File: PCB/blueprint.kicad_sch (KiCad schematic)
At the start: 7 parts, among them SW1 SW_Push, SW2 SW_Push, SW3 SW_Push, SW4 SW_Push, U1 XIAO-RP2040-DIP

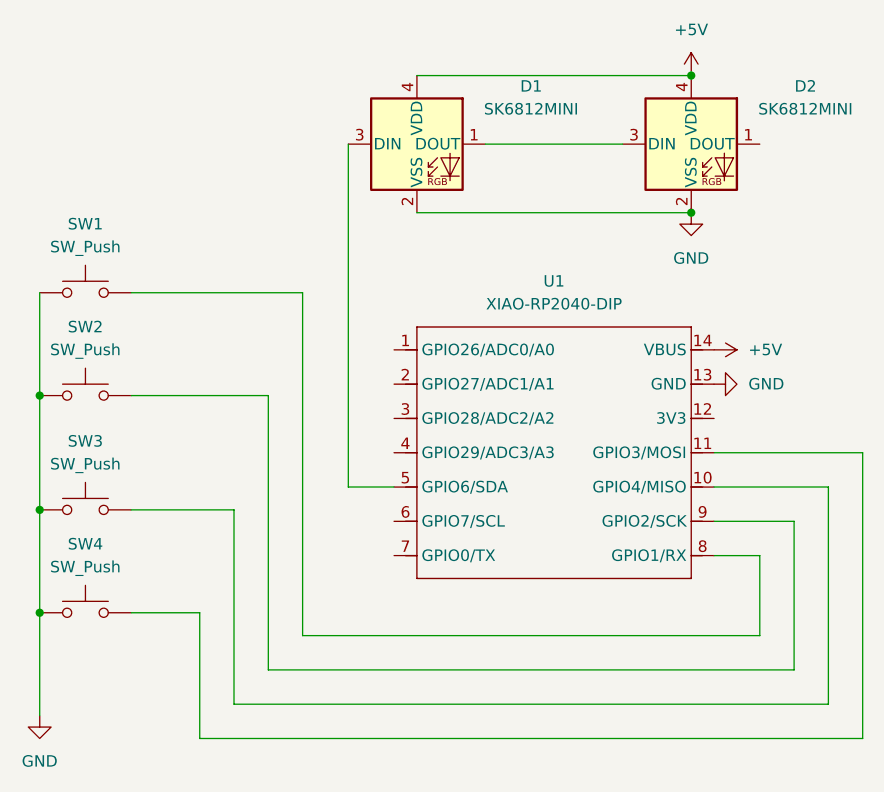
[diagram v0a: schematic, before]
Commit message: Updated CAD and PCB for new Bear Case and layout
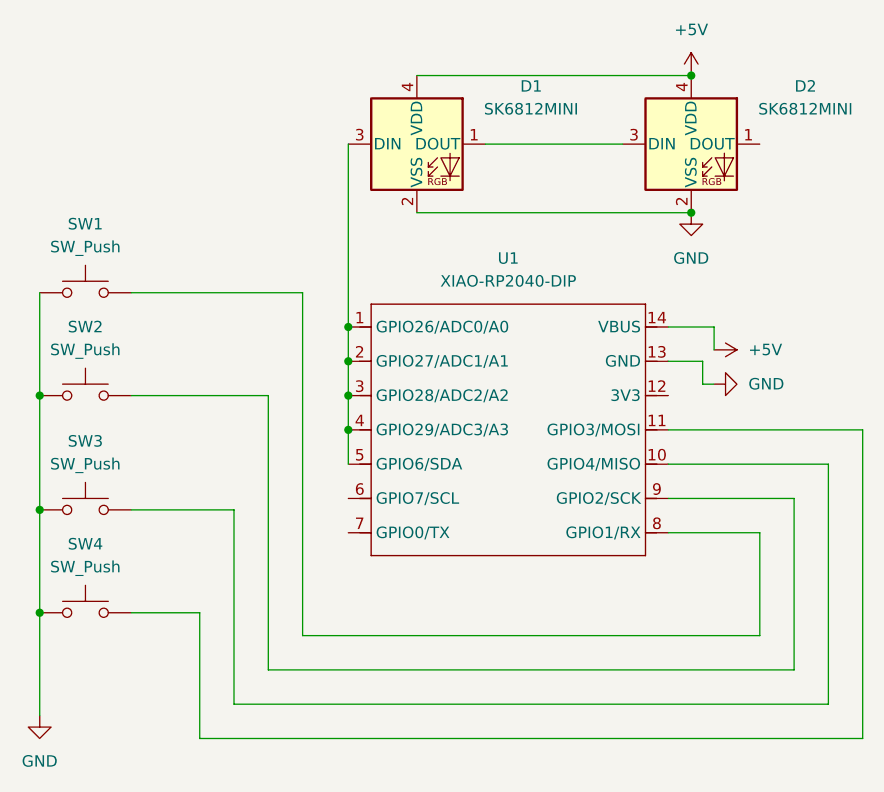
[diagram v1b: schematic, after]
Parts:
- U1: footprint Module:MOUDLE14P-XIAO-DIP-SMD -> OPL Library:XIAO-RP2040-DIP
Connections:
- net at U1.1 (GPIO26/ADC0/A0): now also D1.3 (DIN), U1.2 (GPIO27/ADC1/A1), U1.3 (GPIO28/ADC2/A2), U1.4 (GPIO29/ADC3/A3), U1.5 (GPIO6/SDA)
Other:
- moved on the sheet: U1
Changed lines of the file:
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@@
+	)
+	(junction
+		(at 93.98 74.93)
+		(diameter 0)
+		(color 0 0 0 0)
 	)
 	(junction
@@
 		(color 0 0 0 0)
 	)
-	(wire
-		(pts
-			(xy 147.32 105.41) (xy 147.32 81.28)
+	(junction
+		(at 93.98 63.5)
+		(diameter 0)
+		(color 0 0 0 0)
+	)
+	(junction
+		(at 93.98 71.12)
+		(diameter 0)
+		(color 0 0 0 0)
+	)
+	(junction
+		(at 93.98 67.31)
+		(diameter 0)
+		(color 0 0 0 0)
+	)
+	(wire
+		(pts
+			(xy 147.32 105.41) (xy 147.32 78.74)
 		)
 		(stroke
@@
 	(wire
 		(pts
-			(xy 139.7 97.79) (xy 139.7 88.9)
+			(xy 139.7 97.79) (xy 139.7 86.36)
 		)
 		(stroke
@@
 	(wire
 		(pts
-			(xy 151.13 77.47) (xy 134.62 77.47)
-		)
-		(stroke
-			(width 0)
-			(type default)
-		)
-	)
-	(wire
-		(pts
-			(xy 93.98 43.18) (xy 93.98 81.28)
-		)
-		(stroke
-			(width 0)
-			(type default)
-		)
-	)
-	(wire
-		(pts
-			(xy 151.13 109.22) (xy 151.13 77.47)
+			(xy 93.98 71.12) (xy 93.98 74.93)
+		)
+		(stroke
+			(width 0)
+			(type default)
+		)
+	)
+	(wire
+		(pts
+			(xy 151.13 74.93) (xy 129.54 74.93)
+		)
+		(stroke
+			(width 0)
+			(type default)
+		)
+	)
+	(wire
+		(pts
+			(xy 93.98 63.5) (xy 93.98 67.31)
+		)
+		(stroke
+			(width 0)
+			(type default)
+		)
+	)
+	(wire
+		(pts
+			(xy 93.98 43.18) (xy 93.98 63.5)
+		)
+		(stroke
+			(width 0)
+			(type default)
+		)
+	)
+	(wire
+		(pts
+			(xy 129.54 63.5) (xy 134.62 63.5)
+		)
+		(stroke
+			(width 0)
+			(type default)
+		)
+	)
+	(wire
+		(pts
+			(xy 151.13 109.22) (xy 151.13 74.93)
+		)
+		(stroke
+			(width 0)
+			(type default)
+		)
+	)
+	(wire
+		(pts
+			(xy 93.98 67.31) (xy 93.98 71.12)
+		)
+		(stroke
+			(width 0)
+			(type default)
+		)
+	)
+	(wire
+		(pts
+			(xy 133.35 69.85) (xy 134.62 69.85)
 		)
 		(stroke
@@
 	(wire
 		(pts
-			(xy 134.62 81.28) (xy 147.32 81.28)
+			(xy 129.54 78.74) (xy 147.32 78.74)
 		)
 		(stroke
@@
 	(wire
 		(pts
-			(xy 93.98 81.28) (xy 99.06 81.28)
-		)
-		(stroke
-			(width 0)
-			(type default)
-		)
-	)
-	(wire
-		(pts
 			(xy 77.47 95.25) (xy 77.47 109.22)
 		)
@@
 	(wire
 		(pts
+			(xy 133.35 67.31) (xy 133.35 69.85)
+		)
+		(stroke
+			(width 0)
+			(type default)
+		)
+	)
+	(wire
+		(pts
 			(xy 81.28 105.41) (xy 147.32 105.41)
 		)
@@
 	(wire
 		(pts
-			(xy 143.51 101.6) (xy 143.51 85.09)
-		)
-		(stroke
-			(width 0)
-			(type default)
-		)
-	)
-	(wire
-		(pts
-			(xy 139.7 88.9) (xy 134.62 88.9)
+			(xy 143.51 101.6) (xy 143.51 82.55)
+		)
+		(stroke
+			(width 0)
+			(type default)
+		)
+	)
+	(wire
+		(pts
+			(xy 129.54 67.31) (xy 133.35 67.31)
+		)
+		(stroke
+			(width 0)
+			(type default)
+		)
+	)
+	(wire
+		(pts
+			(xy 139.7 86.36) (xy 129.54 86.36)
+		)
+		(stroke
+			(width 0)
+			(type default)
+		)
+	)
+	(wire
+		(pts
+			(xy 93.98 74.93) (xy 93.98 78.74)
 		)
 		(stroke
@@
 	(wire
 		(pts
-			(xy 134.62 85.09) (xy 143.51 85.09)
+			(xy 134.62 63.5) (xy 134.62 66.04)
+		)
+		(stroke
+			(width 0)
+			(type default)
+		)
+	)
+	(wire
+		(pts
+			(xy 129.54 82.55) (xy 143.51 82.55)
 		)
 		(stroke
@@
 	(symbol
 		(lib_id "OPL Library:XIAO-RP2040-DIP")
-		(at 102.87 60.96 0)
+		(at 97.79 58.42 0)
 		(unit 1)
 		(exclude_from_sim no)
@@
 		(fields_autoplaced yes)
 		(property "Reference" "U1"
-			(at 116.84 58.42 0)
+			(at 111.76 55.88 0)
 			(effects
 				(font
@@
 		)
 		(property "Value" "XIAO-RP2040-DIP"
-			(at 116.84 60.96 0)
+			(at 111.76 58.42 0)
 			(effects
 				(font
@@
 			)
 		)
-		(property "Footprint" "Module:MOUDLE14P-XIAO-DIP-SMD"
-			(at 117.348 93.218 0)
+		(property "Footprint" "OPL Library:XIAO-RP2040-DIP"
+			(at 112.268 90.678 0)
 			(effects
 				(font
@@
 		)
 		(property "Datasheet" ""
-			(at 102.87 60.96 0)
+			(at 97.79 58.42 0)
 			(effects
 				(font
@@
 		)
 		(property "Description" ""
-			(at 102.87 60.96 0)
+			(at 97.79 58.42 0)
 			(effects
 				(font
